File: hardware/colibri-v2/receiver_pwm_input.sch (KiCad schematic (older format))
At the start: 11 parts, among them P18 CONN_01X03, P19 CONN_01X03, P20 CONN_01X03, P21 CONN_01X03, P22 CONN_01X03, U19 SN74LVC162244A

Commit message: Work on cortex USB connection.
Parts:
- renumbered P18 to P?, P19 to P?, P20 to P?, P21 to P?, P22 to P?, R136 to R?, R137 to R?, R138 to R?, R139 to R?, R140 to R?, U19 to U?
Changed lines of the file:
@@
 Can we have 22 OHM \nresistors here?
 $Comp
-L CONN_01X03 P18
+L CONN_01X03 P?
 U 1 1 5624B1D9
 P 7250 1550
-F 0 "P18" H 7250 1750 50  0000 C CNN
+F 0 "P?" H 7250 1750 50  0000 C CNN
 F 1 "CONN_01X03" V 7350 1550 50  0000 C CNN
 F 2 "" H 7250 1550 60  0001 C CNN
@@
 $EndComp
 $Comp
-L +5V #PWR0182
+L +5V #PWR?
 U 1 1 5624B1E0
 P 6900 1350
-F 0 "#PWR0182" H 6900 1200 50  0001 C CNN
+F 0 "#PWR?" H 6900 1200 50  0001 C CNN
 F 1 "+5V" H 6900 1490 50  0000 C CNN
 F 2 "" H 6900 1350 60  0000 C CNN
@@
 $EndComp
 $Comp
-L GND #PWR0183
+L GND #PWR?
 U 1 1 5624B1E6
 P 6900 1750
-F 0 "#PWR0183" H 6900 1500 50  0001 C CNN
+F 0 "#PWR?" H 6900 1500 50  0001 C CNN
 F 1 "GND" H 6900 1600 50  0000 C CNN
 F 2 "" H 6900 1750 60  0000 C CNN
@@
 $EndComp
 $Comp
-L R R136
+L R R?
 U 1 1 5624B1EC
 P 6500 1450
-F 0 "R136" V 6580 1450 50  0000 C CNN
+F 0 "R?" V 6580 1450 50  0000 C CNN
 F 1 "100" V 6500 1450 50  0000 C CNN
 F 2 "Resistors_SMD:R_0603" V 6430 1450 30  0001 C CNN
@@
 $EndComp
 $Comp
-L CONN_01X03 P19
+L CONN_01X03 P?
 U 1 1 5624B1F9
 P 7250 2450
-F 0 "P19" H 7250 2650 50  0000 C CNN
+F 0 "P?" H 7250 2650 50  0000 C CNN
 F 1 "CONN_01X03" V 7350 2450 50  0000 C CNN
 F 2 "" H 7250 2450 60  0001 C CNN
@@
 $EndComp
 $Comp
-L +5V #PWR0184
+L +5V #PWR?
 U 1 1 5624B200
 P 6900 2250
-F 0 "#PWR0184" H 6900 2100 50  0001 C CNN
+F 0 "#PWR?" H 6900 2100 50  0001 C CNN
 F 1 "+5V" H 6900 2390 50  0000 C CNN
 F 2 "" H 6900 2250 60  0000 C CNN
@@
 $EndComp
 $Comp
-L GND #PWR0185
+L GND #PWR?
 U 1 1 5624B206
 P 6900 2650
-F 0 "#PWR0185" H 6900 2400 50  0001 C CNN
+F 0 "#PWR?" H 6900 2400 50  0001 C CNN
 F 1 "GND" H 6900 2500 50  0000 C CNN
 F 2 "" H 6900 2650 60  0000 C CNN
@@
 $EndComp
 $Comp
-L R R137
+L R R?
 U 1 1 5624B20C
 P 6500 2350
-F 0 "R137" V 6580 2350 50  0000 C CNN
+F 0 "R?" V 6580 2350 50  0000 C CNN
 F 1 "100" V 6500 2350 50  0000 C CNN
 F 2 "Resistors_SMD:R_0603" V 6430 2350 30  0001 C CNN
@@
 $EndComp
 $Comp
-L CONN_01X03 P20
+L CONN_01X03 P?
 U 1 1 5624B219
 P 7250 3350
-F 0 "P20" H 7250 3550 50  0000 C CNN
+F 0 "P?" H 7250 3550 50  0000 C CNN
 F 1 "CONN_01X03" V 7350 3350 50  0000 C CNN
 F 2 "" H 7250 3350 60  0001 C CNN
@@
 $EndComp
 $Comp
-L +5V #PWR0186
+L +5V #PWR?
 U 1 1 5624B220
 P 6900 3150
-F 0 "#PWR0186" H 6900 3000 50  0001 C CNN
+F 0 "#PWR?" H 6900 3000 50  0001 C CNN
 F 1 "+5V" H 6900 3290 50  0000 C CNN
 F 2 "" H 6900 3150 60  0000 C CNN
@@
 $EndComp
 $Comp
-L GND #PWR0187
+L GND #PWR?
 U 1 1 5624B226
 P 6900 3550
-F 0 "#PWR0187" H 6900 3300 50  0001 C CNN
+F 0 "#PWR?" H 6900 3300 50  0001 C CNN
 F 1 "GND" H 6900 3400 50  0000 C CNN
 F 2 "" H 6900 3550 60  0000 C CNN
@@
 $EndComp
 $Comp
-L R R138
+L R R?
 U 1 1 5624B22C
 P 6500 3250
-F 0 "R138" V 6580 3250 50  0000 C CNN
+F 0 "R?" V 6580 3250 50  0000 C CNN
 F 1 "100" V 6500 3250 50  0000 C CNN
 F 2 "Resistors_SMD:R_0603" V 6430 3250 30  0001 C CNN
@@
 $EndComp
 $Comp
-L CONN_01X03 P21
+L CONN_01X03 P?
 U 1 1 5624B239
 P 7250 4250
-F 0 "P21" H 7250 4450 50  0000 C CNN
+F 0 "P?" H 7250 4450 50  0000 C CNN
 F 1 "CONN_01X03" V 7350 4250 50  0000 C CNN
 F 2 "" H 7250 4250 60  0001 C CNN
@@
 $EndComp
 $Comp
-L +5V #PWR0188
+L +5V #PWR?
 U 1 1 5624B240
 P 6900 4050
-F 0 "#PWR0188" H 6900 3900 50  0001 C CNN
+F 0 "#PWR?" H 6900 3900 50  0001 C CNN
 F 1 "+5V" H 6900 4190 50  0000 C CNN
 F 2 "" H 6900 4050 60  0000 C CNN
@@
 $EndComp
 $Comp
-L GND #PWR0189
+L GND #PWR?
 U 1 1 5624B246
 P 6900 4450
-F 0 "#PWR0189" H 6900 4200 50  0001 C CNN
+F 0 "#PWR?" H 6900 4200 50  0001 C CNN
 F 1 "GND" H 6900 4300 50  0000 C CNN
 F 2 "" H 6900 4450 60  0000 C CNN
@@
 $EndComp
 $Comp
-L R R139
+L R R?
 U 1 1 5624B24C
 P 6500 4150
-F 0 "R139" V 6580 4150 50  0000 C CNN
+F 0 "R?" V 6580 4150 50  0000 C CNN
 F 1 "100" V 6500 4150 50  0000 C CNN
 F 2 "Resistors_SMD:R_0603" V 6430 4150 30  0001 C CNN
@@
 $EndComp
 $Comp
-L SN74LVC162244A U19
-U 4 1 5624B259
+L SN74LVC162244A U?
+U 1 1 5624B259
 P 4950 3050
-F 0 "U19" H 5150 3600 60  0000 C CNN
+F 0 "U?" H 5150 3600 60  0000 C CNN
 F 1 "SN74LVC162244A" H 4950 2500 60  0000 C CNN
 F 2 "" H 4950 2900 60  0001 C CNN
 F 3 "" H 4950 2900 60  0000 C CNN
-	4    4950 3050
+	1    4950 3050
 	-1   0    0    -1
 $EndComp
@@
 RCV_PWM_4
 $Comp
-L CONN_01X03 P22
+L CONN_01X03 P?
 U 1 1 5624BF56
 P 7250 5300
-F 0 "P22" H 7250 5500 50  0000 C CNN
+F 0 "P?" H 7250 5500 50  0000 C CNN
 F 1 "CONN_01X03" V 7350 5300 50  0000 C CNN
 F 2 "" H 7250 5300 60  0001 C CNN
@@
 $EndComp
 $Comp
-L +5V #PWR0190
+L +5V #PWR?
 U 1 1 5624BF5C
 P 6900 5100
-F 0 "#PWR0190" H 6900 4950 50  0001 C CNN
+F 0 "#PWR?" H 6900 4950 50  0001 C CNN
 F 1 "+5V" H 6900 5240 50  0000 C CNN
 F 2 "" H 6900 5100 60  0000 C CNN
@@
 $EndComp
 $Comp
-L GND #PWR0191
+L GND #PWR?
 U 1 1 5624BF62
 P 6900 5500
-F 0 "#PWR0191" H 6900 5250 50  0001 C CNN
+F 0 "#PWR?" H 6900 5250 50  0001 C CNN
 F 1 "GND" H 6900 5350 50  0000 C CNN
 F 2 "" H 6900 5500 60  0000 C CNN
@@
 $EndComp
 $Comp
-L R R140
+L R R?
 U 1 1 5624BF68
 P 6500 5200
-F 0 "R140" V 6580 5200 50  0000 C CNN
+F 0 "R?" V 6580 5200 50  0000 C CNN
 F 1 "100" V 6500 5200 50  0000 C CNN
 F 2 "Resistors_SMD:R_0603" V 6430 5200 30  0001 C CNN
@@
 $EndComp
 $Comp
-L GND #PWR0192
+L GND #PWR?
 U 1 1 5624BFB9
 P 4400 8350
-F 0 "#PWR0192" H 4400 8100 50  0001 C CNN
+F 0 "#PWR?" H 4400 8100 50  0001 C CNN
 F 1 "GND" H 4400 8200 50  0000 C CNN
 F 2 "" H 4400 8350 60  0000 C CNN
@@
 $EndComp
 $Comp
-L SN74LVC162244A U19
-U 5 1 5624BFCA
+L SN74LVC162244A U?
+U 1 1 5624BFCA
 P 4950 5400
-F 0 "U19" H 5150 5950 60  0000 C CNN
+F 0 "U?" H 5150 5950 60  0000 C CNN
 F 1 "SN74LVC162244A" H 4950 4850 60  0000 C CNN
 F 2 "" H 4950 5250 60  0001 C CNN
 F 3 "" H 4950 5250 60  0000 C CNN
-	5    4950 5400
+	1    4950 5400
 	-1   0    0    -1
 $EndComp
 $Comp
-L GND #PWR0193
+L GND #PWR?
 U 1 1 5624BFE2
 P 5650 5000
-F 0 "#PWR0193" H 5650 4750 50  0001 C CNN
+F 0 "#PWR?" H 5650 4750 50  0001 C CNN
 F 1 "GND" H 5650 4850 50  0000 C CNN
 F 2 "" H 5650 5000 60  0000 C CNN
@@
 	5400 5000 5650 5000
 $Comp
-L GND #PWR0194
+L GND #PWR?
 U 1 1 5624F657
 P 5650 2650
-F 0 "#PWR0194" H 5650 2400 50  0001 C CNN
+F 0 "#PWR?" H 5650 2400 50  0001 C CNN
 F 1 "GND" H 5650 2500 50  0000 C CNN
 F 2 "" H 5650 2650 60  0000 C CNN

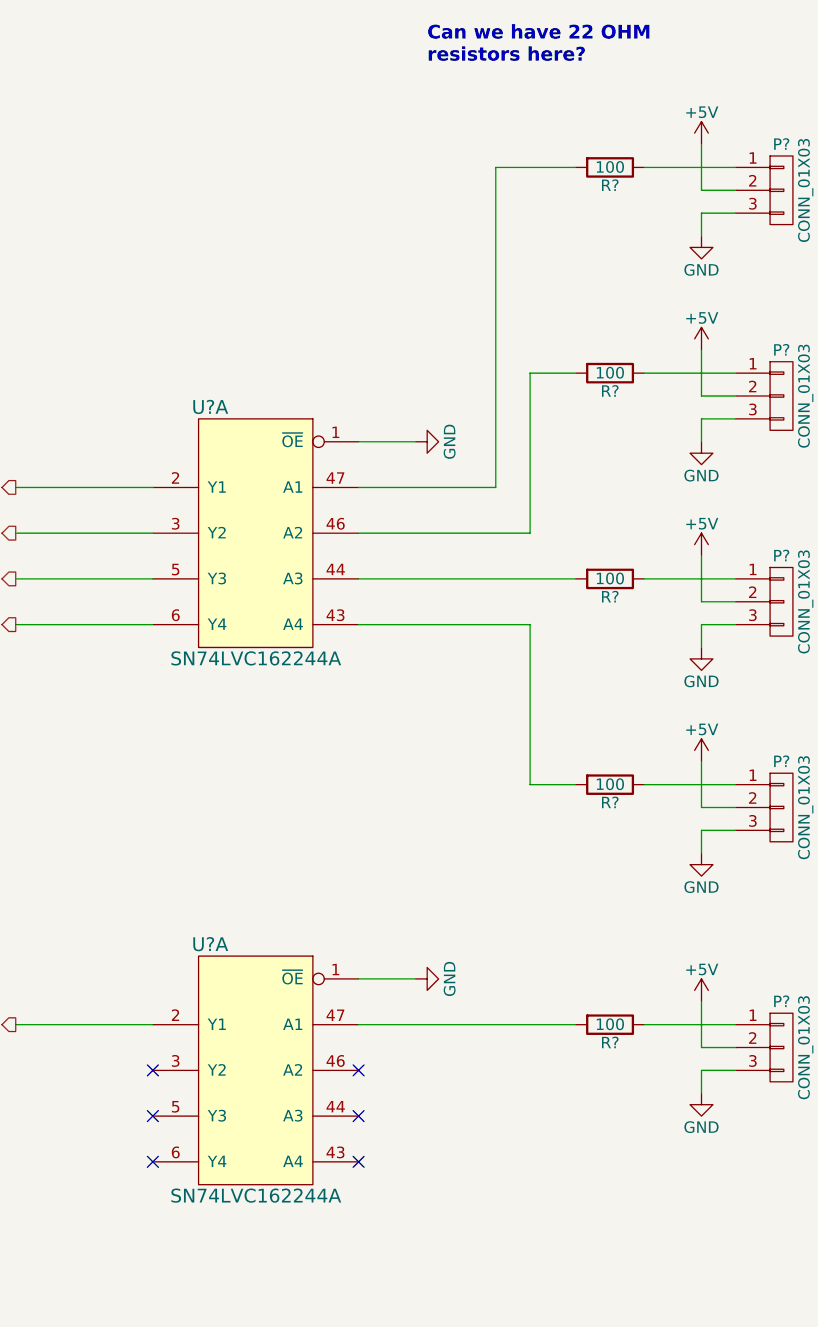
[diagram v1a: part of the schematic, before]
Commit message: Work on wandboard lcd and usb
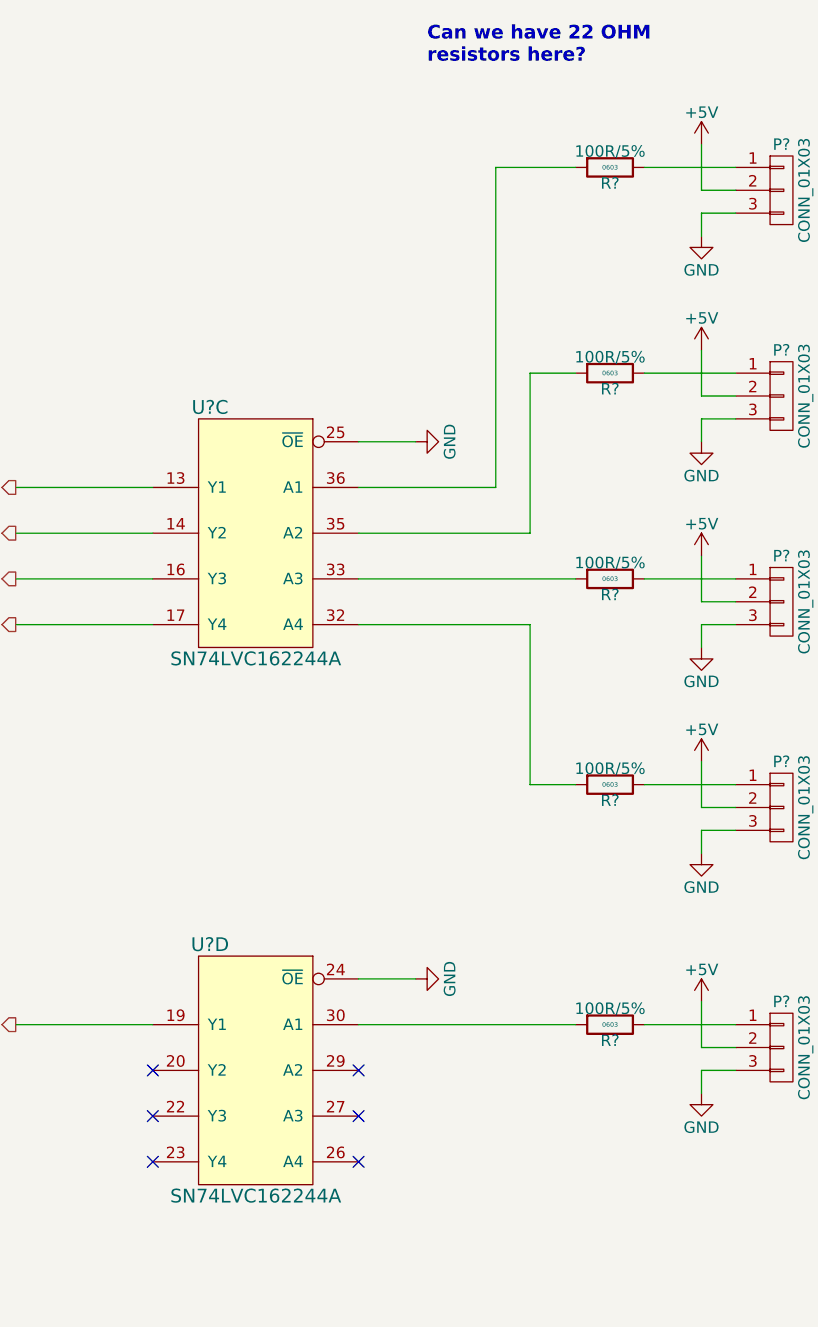
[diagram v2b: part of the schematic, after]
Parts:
- removed R? (x5): 100, Resistors_SMD:R_0603, symbol R
- added R? (x5): 100R/5%, Resistors_SMD:R_0603, symbol R_SMT
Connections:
- net GND: now also U?.24 (~OE), U?.25 (~OE); no longer U?.1 (~OE), U?.1 (~OE)
- net RCV_PWM_0: now also U?.13 (Y1); no longer U?.2 (Y1)
- net RCV_PWM_1: now also U?.14 (Y2); no longer U?.3 (Y2)
- net RCV_PWM_2: now also U?.16 (Y3); no longer U?.5 (Y3)
- net RCV_PWM_3: now also U?.17 (Y4); no longer U?.6 (Y4)
- net RCV_PWM_4: now also U?.19 (Y1); no longer U?.2 (Y1)
- net at P?.1 (P1): now also R?.1 (x5)
- new net: R?.2, U?.32 (A4)
- new net: R?.2, U?.33 (A3)
- new net: R?.2, U?.35 (A2)
- new net: R?.2, U?.36 (A1)
- new net: R?.2, U?.30 (A1)
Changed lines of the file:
@@
-$EndComp
-$Comp
-L R R?
-U 1 1 5624B1EC
-P 6500 1450
-F 0 "R?" V 6580 1450 50  0000 C CNN
-F 1 "100" V 6500 1450 50  0000 C CNN
-F 2 "Resistors_SMD:R_0603" V 6430 1450 30  0001 C CNN
-F 3 "" H 6500 1450 30  0000 C CNN
-	1    6500 1450
-	0    1    1    0
 $EndComp
 $Comp
@@
 $EndComp
 $Comp
-L R R?
-U 1 1 5624B20C
-P 6500 2350
-F 0 "R?" V 6580 2350 50  0000 C CNN
-F 1 "100" V 6500 2350 50  0000 C CNN
-F 2 "Resistors_SMD:R_0603" V 6430 2350 30  0001 C CNN
-F 3 "" H 6500 2350 30  0000 C CNN
-	1    6500 2350
-	0    1    1    0
-$EndComp
-$Comp
 L CONN_01X03 P?
 U 1 1 5624B219
@@
 $EndComp
 $Comp
-L R R?
-U 1 1 5624B22C
-P 6500 3250
-F 0 "R?" V 6580 3250 50  0000 C CNN
-F 1 "100" V 6500 3250 50  0000 C CNN
-F 2 "Resistors_SMD:R_0603" V 6430 3250 30  0001 C CNN
-F 3 "" H 6500 3250 30  0000 C CNN
-	1    6500 3250
-	0    1    1    0
-$EndComp
-$Comp
 L CONN_01X03 P?
 U 1 1 5624B239
@@
 $EndComp
 $Comp
-L R R?
-U 1 1 5624B24C
-P 6500 4150
-F 0 "R?" V 6580 4150 50  0000 C CNN
-F 1 "100" V 6500 4150 50  0000 C CNN
-F 2 "Resistors_SMD:R_0603" V 6430 4150 30  0001 C CNN
-F 3 "" H 6500 4150 30  0000 C CNN
-	1    6500 4150
-	0    1    1    0
-$EndComp
-$Comp
 L SN74LVC162244A U?
-U 1 1 5624B259
+U 3 1 5624B259
 P 4950 3050
 F 0 "U?" H 5150 3600 60  0000 C CNN
@@
 F 2 "" H 4950 2900 60  0001 C CNN
 F 3 "" H 4950 2900 60  0000 C CNN
-	1    4950 3050
+	3    4950 3050
 	-1   0    0    -1
 $EndComp
@@
 $EndComp
 $Comp
-L R R?
-U 1 1 5624BF68
-P 6500 5200
-F 0 "R?" V 6580 5200 50  0000 C CNN
-F 1 "100" V 6500 5200 50  0000 C CNN
-F 2 "Resistors_SMD:R_0603" V 6430 5200 30  0001 C CNN
-F 3 "" H 6500 5200 30  0000 C CNN
-	1    6500 5200
-	0    1    1    0
-$EndComp
-$Comp
 L GND #PWR?
 U 1 1 5624BFB9
@@
 $Comp
 L SN74LVC162244A U?
-U 1 1 5624BFCA
+U 4 1 5624BFCA
 P 4950 5400
 F 0 "U?" H 5150 5950 60  0000 C CNN
@@
 F 2 "" H 4950 5250 60  0001 C CNN
 F 3 "" H 4950 5250 60  0000 C CNN
-	1    4950 5400
+	4    4950 5400
 	-1   0    0    -1
 $EndComp
@@
 Wire Wire Line
 	5400 2650 5650 2650
+$Comp
+L R_SMT R?
+U 1 1 5633EFE8
+P 6500 5200
+F 0 "R?" V 6570 5200 50  0000 C CNN
+F 1 "100R/5%" V 6430 5200 50  0000 C CNN
+F 2 "Resistors_SMD:R_0603" V 6650 5200 30  0001 C CNN
+F 3 "" V 6580 5200 30  0000 C CNN
+F 4 "0603" V 6500 5200 20  0000 C CNN "SMT"
+F 5 "9331689" V 6700 5200 30  0001 C CNN "Part"
+F 6 "Farnell" V 6750 5200 30  0001 C CNN "Provider"
+	1    6500 5200
+	0    1    1    0
+$EndComp
+$Comp
+L R_SMT R?
+U 1 1 5633F0C4
+P 6500 4150
+F 0 "R?" V 6570 4150 50  0000 C CNN
+F 1 "100R/5%" V 6430 4150 50  0000 C CNN
+F 2 "Resistors_SMD:R_0603" V 6650 4150 30  0001 C CNN
+F 3 "" V 6580 4150 30  0000 C CNN
+F 4 "0603" V 6500 4150 20  0000 C CNN "SMT"
+F 5 "9331689" V 6700 4150 30  0001 C CNN "Part"
+F 6 "Farnell" V 6750 4150 30  0001 C CNN "Provider"
+	1    6500 4150
+	0    1    1    0
+$EndComp
+$Comp
+L R_SMT R?
+U 1 1 5633F136
+P 6500 3250
+F 0 "R?" V 6570 3250 50  0000 C CNN
+F 1 "100R/5%" V 6430 3250 50  0000 C CNN
+F 2 "Resistors_SMD:R_0603" V 6650 3250 30  0001 C CNN
+F 3 "" V 6580 3250 30  0000 C CNN
+F 4 "0603" V 6500 3250 20  0000 C CNN "SMT"
+F 5 "9331689" V 6700 3250 30  0001 C CNN "Part"
+F 6 "Farnell" V 6750 3250 30  0001 C CNN "Provider"
+	1    6500 3250
+	0    1    1    0
+$EndComp
+$Comp
+L R_SMT R?
+U 1 1 5633F18A
+P 6500 2350
+F 0 "R?" V 6570 2350 50  0000 C CNN
+F 1 "100R/5%" V 6430 2350 50  0000 C CNN
+F 2 "Resistors_SMD:R_0603" V 6650 2350 30  0001 C CNN
+F 3 "" V 6580 2350 30  0000 C CNN
+F 4 "0603" V 6500 2350 20  0000 C CNN "SMT"
+F 5 "9331689" V 6700 2350 30  0001 C CNN "Part"
+F 6 "Farnell" V 6750 2350 30  0001 C CNN "Provider"
+	1    6500 2350
+	0    1    1    0
+$EndComp
+$Comp
+L R_SMT R?
+U 1 1 5633F20F
+P 6500 1450
+F 0 "R?" V 6570 1450 50  0000 C CNN
+F 1 "100R/5%" V 6430 1450 50  0000 C CNN
+F 2 "Resistors_SMD:R_0603" V 6650 1450 30  0001 C CNN
+F 3 "" V 6580 1450 30  0000 C CNN
+F 4 "0603" V 6500 1450 20  0000 C CNN "SMT"
+F 5 "9331689" V 6700 1450 30  0001 C CNN "Part"
+F 6 "Farnell" V 6750 1450 30  0001 C CNN "Provider"
+	1    6500 1450
+	0    1    1    0
+$EndComp
 $EndSCHEMATC

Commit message: Work on PWM, USB, MEMS, Power
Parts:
- removed R? (x5): 100R/5%, Resistors_SMD:R_0603, symbol R_SMT
- added R?: 10K/5%, Resistors_SMD:R_0603, symbol R_SMT
- added R?: 0R, Resistors_SMD:R_0603, symbol R_SMT
- added R?: NA, Resistors_SMD:R_0603, symbol R_SMT
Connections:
- net GND: now also R?.1; no longer U?.24 (~OE), U?.25 (~OE)
- net at P?.1 (P1): now also U?.36 (A1)
- net at P?.1 (P1): now also U?.35 (A2)
- net at P?.1 (P1): now also U?.33 (A3)
- net at P?.1 (P1): now also U?.32 (A4)
- net at P?.1 (P1): now also U?.30 (A1)
- new net +3V3: R?.1
- new net PWM_RCV_ENABLE: R?.2
- new net RCV_OE: R?.1, R?.2, R?.2, U?.24 (~OE), U?.25 (~OE)
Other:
- note removed: "Can we have 22 OHM \nresistors here?"
- moved on the sheet: P?, U?C, U?D

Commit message: Work on power conrol sheet
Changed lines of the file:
@@
 	3900 6450 4050 6450
 Wire Wire Line
-	4350 6450 4600 6450
-Wire Wire Line
-	4600 6450 5750 6450
+	4350 6450 5750 6450
 $Comp
 L R_SMT R?
@@
 $EndComp
 Wire Wire Line
-	4600 6250 4600 6450
-Wire Wire Line
-	4600 6450 4600 6650
+	4600 6250 4600 6650
 Connection ~ 4600 6450
 Wire Wire Line
